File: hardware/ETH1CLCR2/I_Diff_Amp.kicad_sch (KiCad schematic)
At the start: 64 parts, among them U1001 MCP6L91T-E/SN, U1002 MCP661-E/SN, U1003 SN74LVC1G3157DBVR, U1004 SN74LVC1G3157DBVR, U1005 MCP661-E/SN, U1006 MCP6L91T-E/SN, U1007 SN74LVC1T45DBV, U1008 SN74LVC1G3157DBVR, U1009 SN74LVC1G3157DBVR, U1010 MCP661-E/SN, U1011 MCP6L91T-E/SN, U1012 SN74LVC1T45DBV

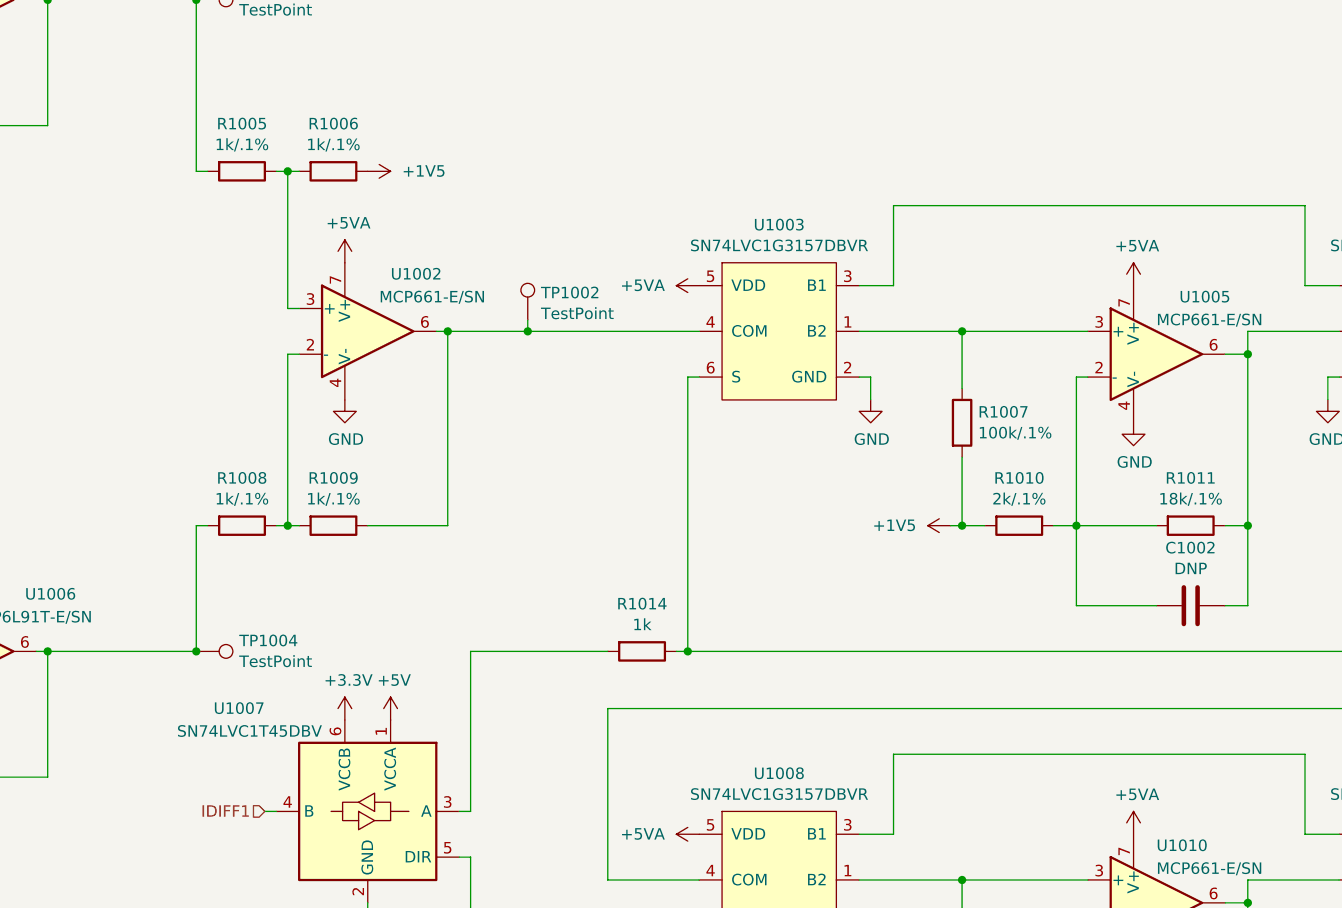
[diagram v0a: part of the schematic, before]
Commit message: Added text to schematics, software development.
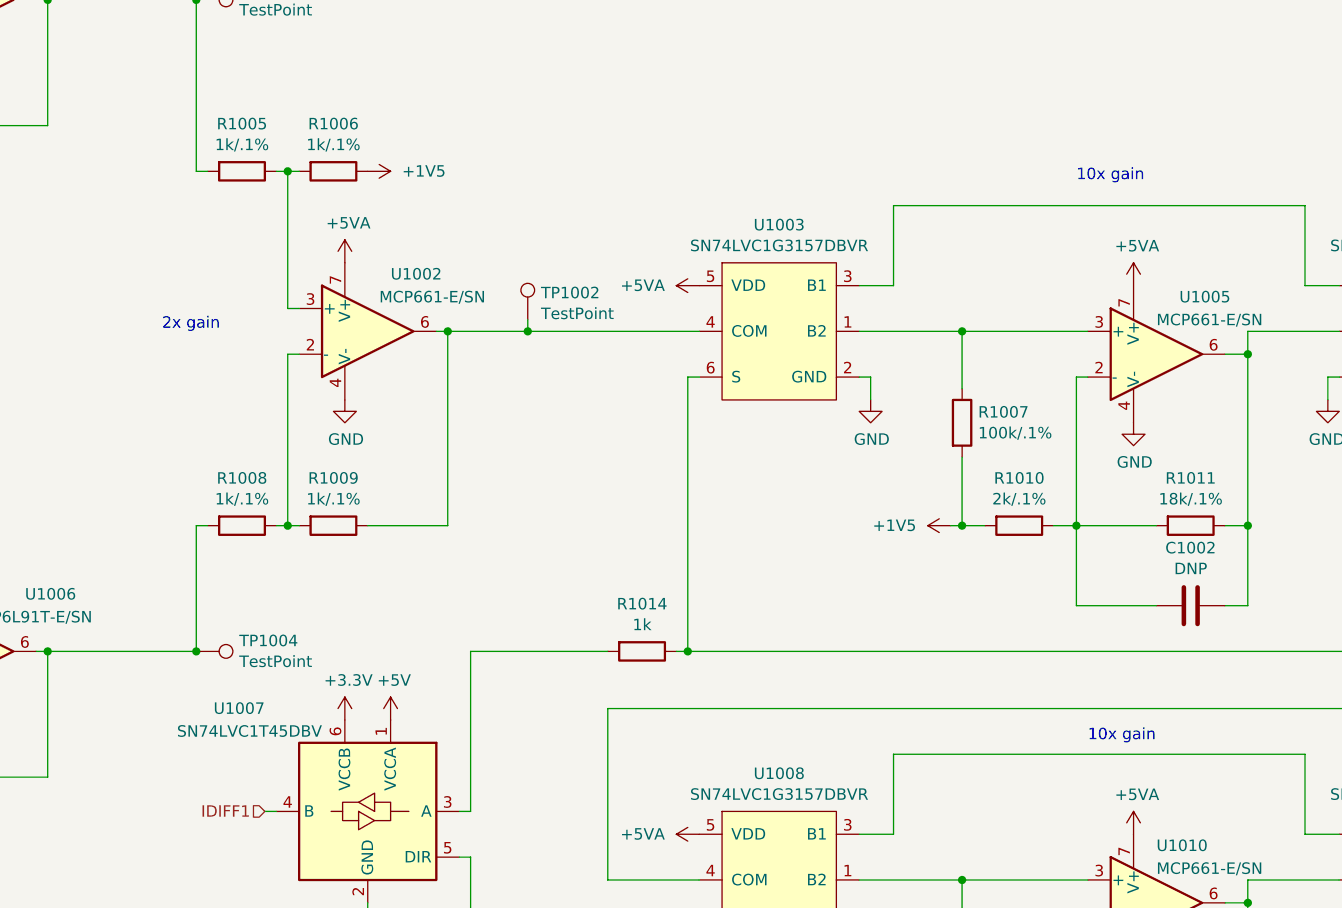
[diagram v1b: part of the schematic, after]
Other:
- note added: "10x gain"
- note added: "2x gain"
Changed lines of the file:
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@@
     (stroke (width 0) (type default) (color 0 0 0 0))
+  )
+  (text "10x gain" (at 250.19 148.59 0)
+    (effects (font (size 1.27 1.27)) (justify left bottom))
+  )
+  (text "10x gain" (at 248.92 86.36 0)
+    (effects (font (size 1.27 1.27)) (justify left bottom))
+  )
+  (text "2x gain" (at 147.32 102.87 0)
+    (effects (font (size 1.27 1.27)) (justify left bottom))
   )
   (hierarchical_label "IDIFF1" (shape input) (at 158.75 156.21 180)
